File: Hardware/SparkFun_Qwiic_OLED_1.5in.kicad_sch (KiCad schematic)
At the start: 39 parts, among them J1 Qwiic_RA, J2 Qwiic_RA, J3 Conn_01x06, J4 Conn_01x24_FPC, U2 WEO128128ASAP3N00000, U5 AP3012

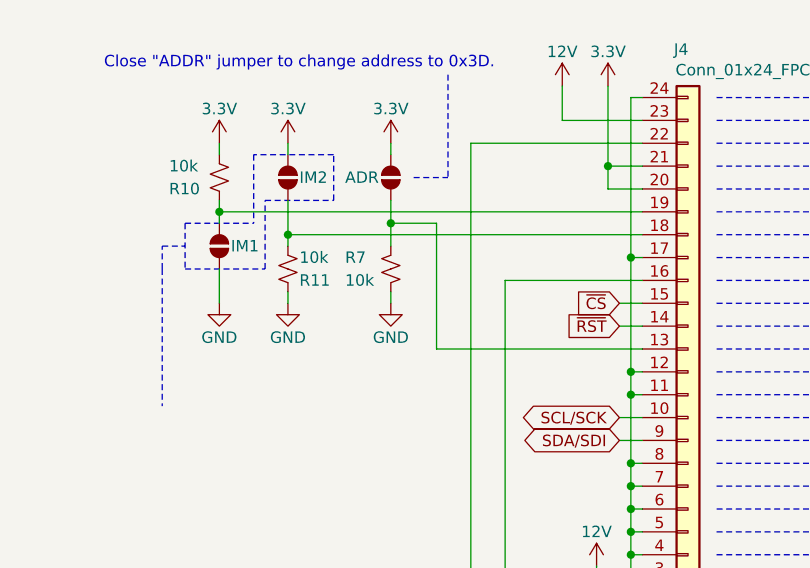
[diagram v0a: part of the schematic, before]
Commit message: Adds no-connect on pin 5, adds prod-id value for 569k resistor
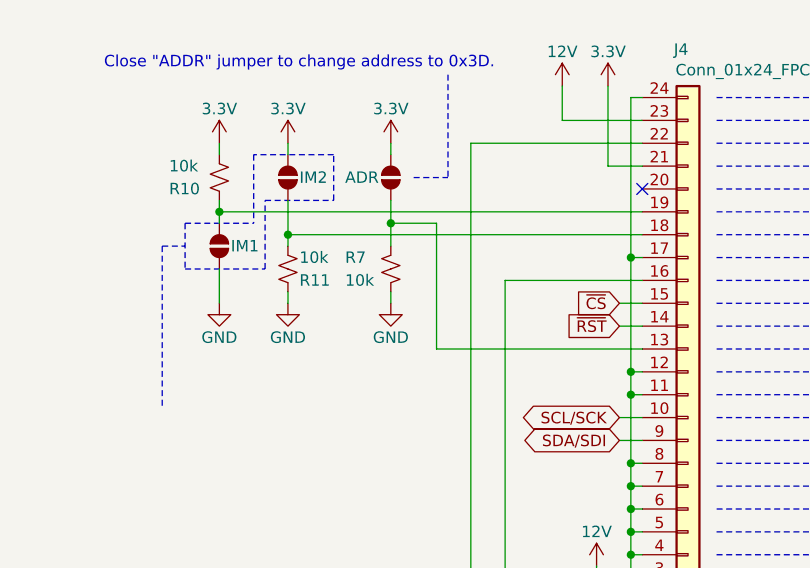
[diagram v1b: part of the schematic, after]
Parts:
- R6: PROD_ID RES-... -> RES-26754
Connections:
- net 3.3V: no longer J4.20 (Pin_20)
- no-connect marks 0 -> 1
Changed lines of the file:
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@@
-	)
-	(junction
-		(at 83.82 44.45)
-		(diameter 0)
-		(color 0 0 0 0)
 	)
 	(junction
@@
 		(color 0 0 0 0)
 	)
+	(no_connect
+		(at 87.63 46.99)
+	)
 	(wire
 		(pts
@@
 	(polyline
 		(pts
-			(xy 34.29 55.88) (xy 34.29 71.12)
+			(xy 34.29 53.34) (xy 34.29 71.12)
 		)
 		(stroke
@@
 	(wire
 		(pts
-			(xy 83.82 46.99) (xy 83.82 44.45)
-		)
-		(stroke
-			(width 0)
-			(type default)
-		)
-	)
-	(wire
-		(pts
 			(xy 83.82 35.56) (xy 83.82 44.45)
 		)
@@
 		)
 	)
-	(polyline
-		(pts
-			(xy 34.29 55.88) (xy 34.29 53.34)
-		)
-		(stroke
-			(width 0)
-			(type dash)
-			(color 132 132 132 1)
-		)
-	)
 	(wire
 		(pts
@@
 			(width 0)
 			(type dash)
-		)
-	)
-	(wire
-		(pts
-			(xy 87.63 46.99) (xy 83.82 46.99)
-		)
-		(stroke
-			(width 0)
-			(type default)
 		)
 	)
@@
 			)
 		)
-		(property "PROD_ID" "RES-..."
+		(property "PROD_ID" "RES-26754"
 			(at 78.74 95.25 0)
 			(effects

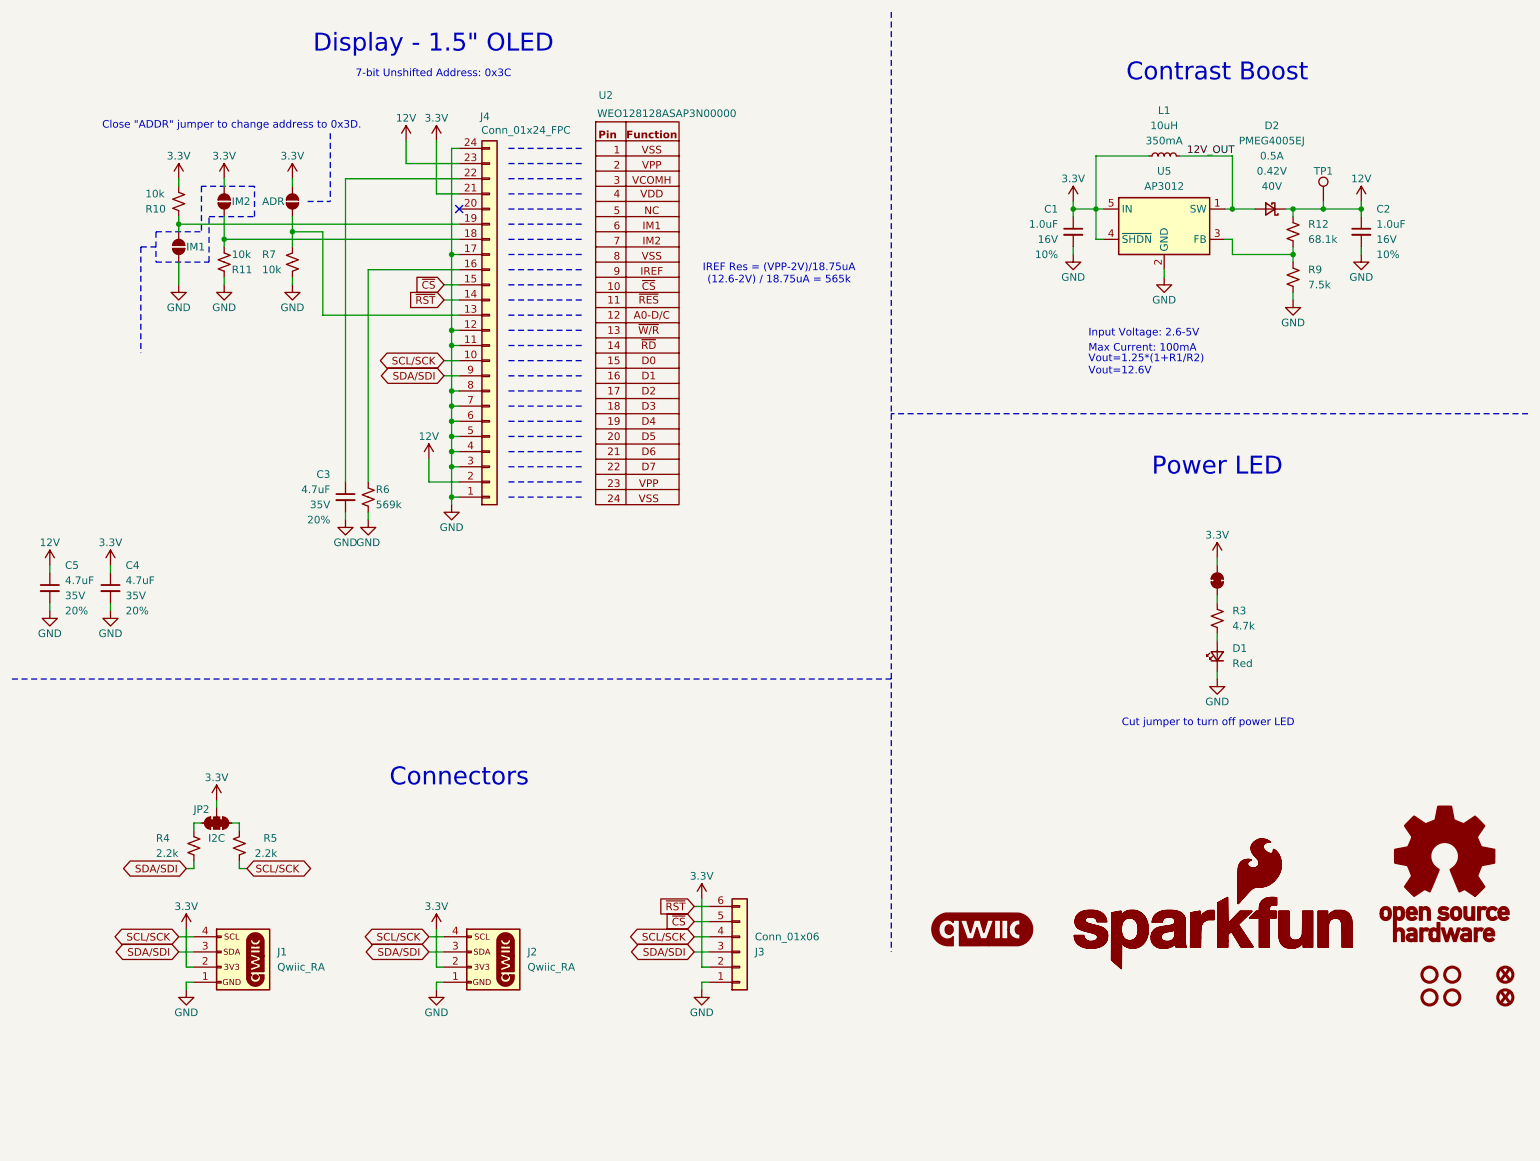
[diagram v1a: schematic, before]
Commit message: Adds D/C to PTH header for SPI funcitonality
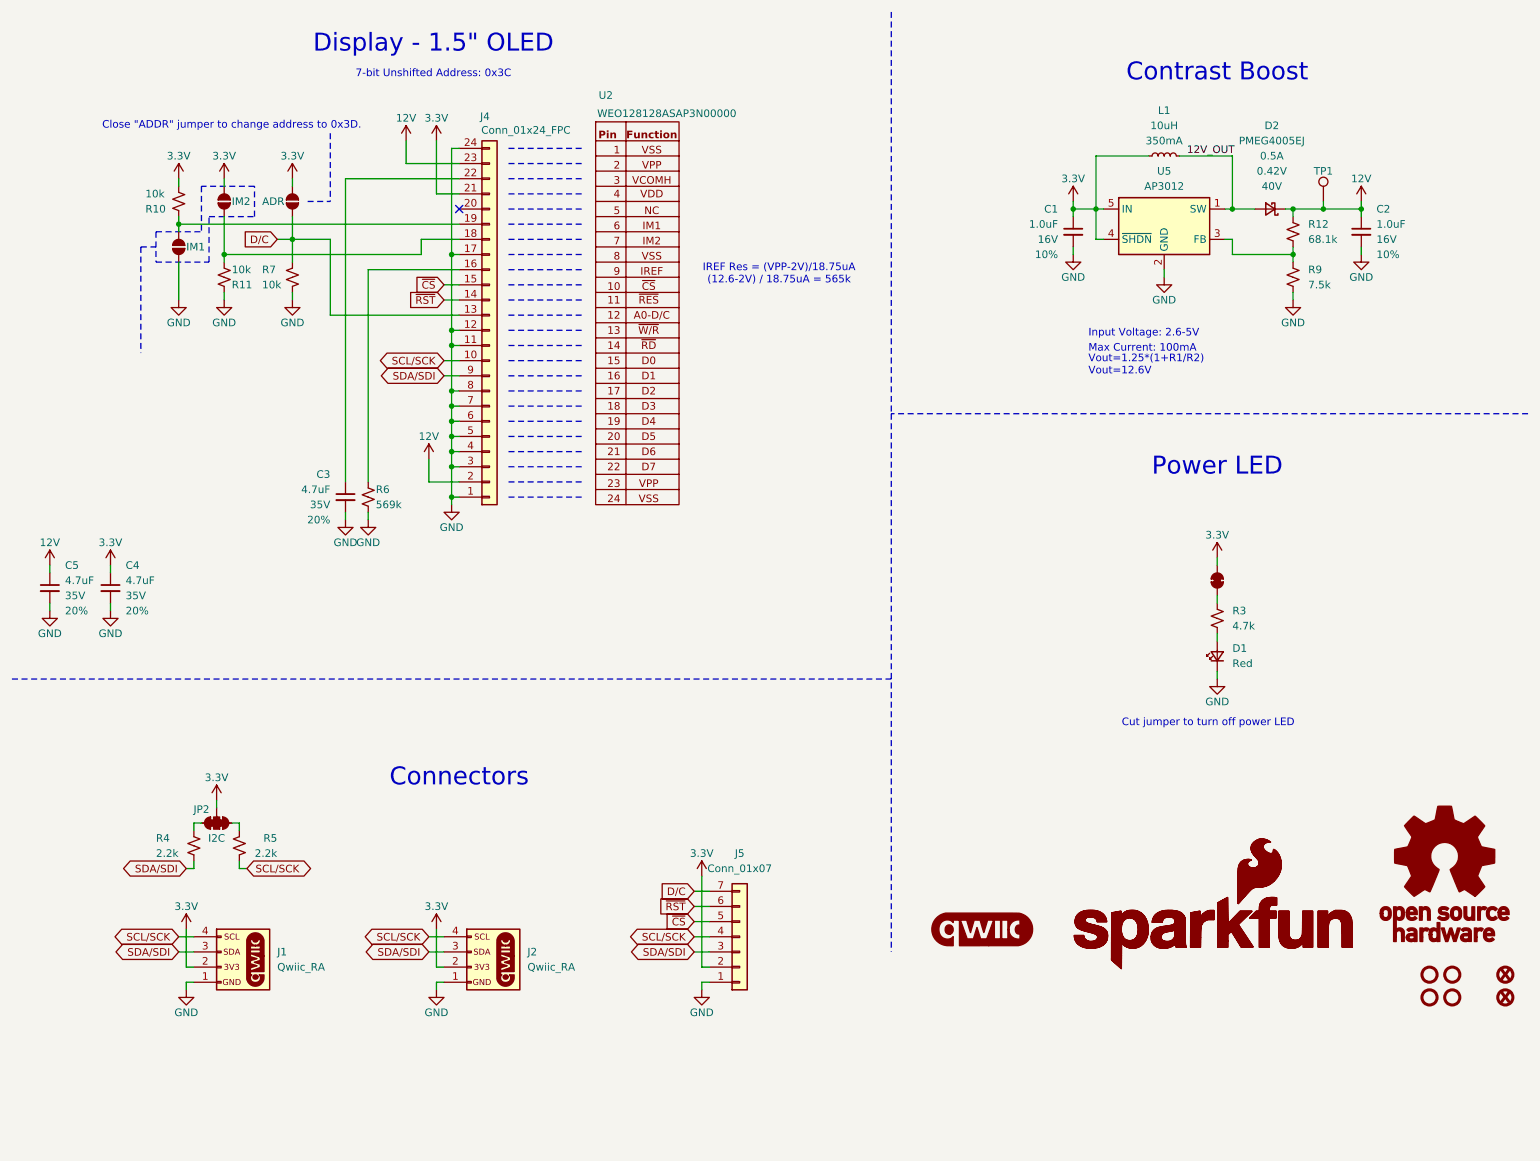
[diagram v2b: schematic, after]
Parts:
- removed J3: Conn_01x06, SparkFun-Connector:1x06, symbol SparkFun-Connector:Conn_01x06
- added J5: Conn_01x07, SparkFun-Connector:1x07, symbol SparkFun-Connector:Conn_01x07
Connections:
- net 3.3V: now also J5.2 (Pin_2)
- net GND: now also J5.1 (Pin_1)
- net SCL/SCK: now also J5.4 (Pin_4)
- net SDA/SDI: now also J5.3 (Pin_3)
- net ~{CS}: now also J5.5 (Pin_5)
- net ~{RST}: now also J5.6 (Pin_6)
- net D/C: now reaches J4.13 (Pin_13), JP3.1 (A), R7.2
- net D/C: now also J5.7 (Pin_7)
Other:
- moved on the sheet: R11, R7

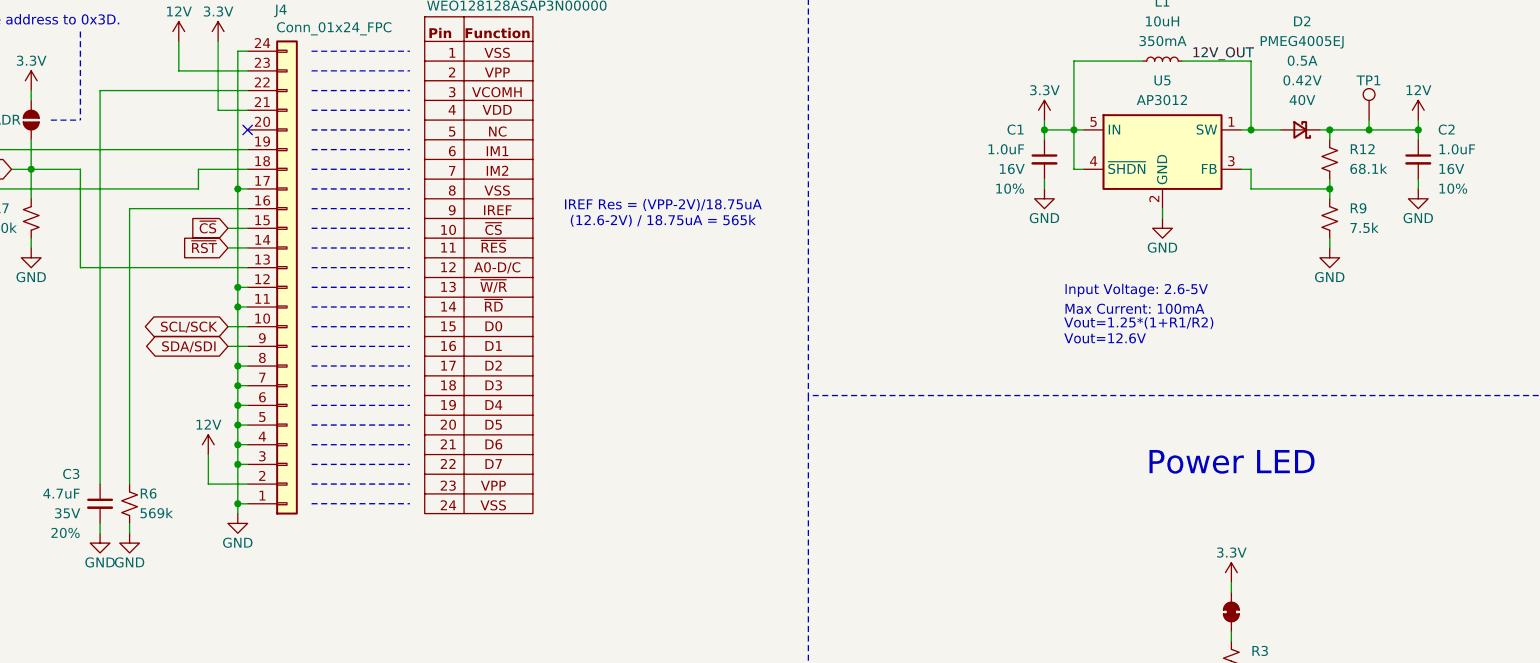
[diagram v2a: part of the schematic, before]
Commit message: Changes certain resistors to use more common values
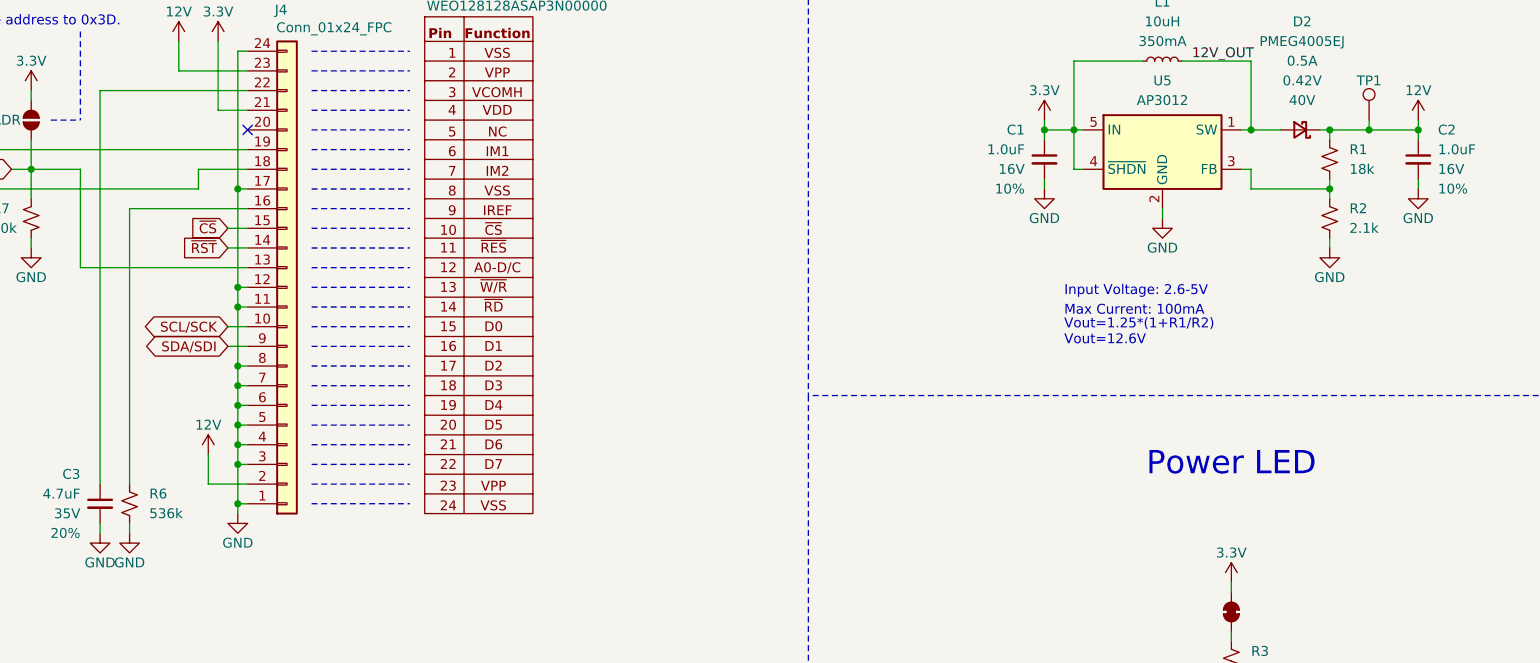
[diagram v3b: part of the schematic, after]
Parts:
- removed R12: 68.1k, SparkFun-Resistor:R_0603_1608Metric, symbol SparkFun-Resistor:68.1k_0603
- removed R6: 569k, SparkFun-Resistor:R_0603_1608Metric, symbol SparkFun-Resistor:634k_0603
- removed R9: 7.5k, SparkFun-Resistor:R_0603_1608Metric, symbol SparkFun-Resistor:7.5k_0603
- added R1: 18k, SparkFun-Resistor:R_0603_1608Metric, symbol SparkFun-Resistor:18k_0603
- added R2: 2.1k, SparkFun-Resistor:R_0603_1608Metric, symbol SparkFun-Resistor:2.1k_0603
- added R6: 536k, SparkFun-Resistor:R_0603_1608Metric, symbol SparkFun-Resistor:536k_0603
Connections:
- net 12V: now also R1.2
- net GND: now also R2.1, R6.1
- net at J4.16 (Pin_16): now also R6.2
- net at U5.3 (FB): now also R1.1, R2.2
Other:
- note removed: "IREF Res = (VPP-2V)/18.75uA (12.6-2V) / 18.75uA = 565k"

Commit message: Updates to v10
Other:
- company: (none) -> SparkFun Electronics
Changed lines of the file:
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@@
 	(title_block
 		(title "SparkFun Qwiic OLED 128x128 1.5in")
-		(date "2025-04-26")
-		(rev "v01")
+		(date "2025-08-06")
+		(rev "v10")
+		(company "SparkFun Electronics")
 		(comment 1 "Designed By: N. Seidle")
 		(comment 2 "Revised By: Elias Santistevan")
@@
 			)
 		)
-		(column_widths 7.62 8.89 13.97)
-		(row_heights 2.54 2.54 2.54)
+		(column_widths 10.16 8.89 13.97)
+		(row_heights 3.81 2.54 2.54 2.54)
 		(cells
 			(table_cell "IM1"
 				(exclude_from_sim no)
 				(at 20.32 71.12 0)
-				(size 7.62 2.54)
+				(size 10.16 3.81)
 				(margins 0.9525 0.9525 0.9525 0.9525)
 				(span 1 1)
@@
 			(table_cell "IM2"
 				(exclude_from_sim no)
-				(at 27.94 71.12 0)
+				(at 30.48 71.12 0)
+				(size 8.89 3.81)
+				(margins 0.9525 0.9525 0.9525 0.9525)
+				(span 1 1)
+				(fill
+					(type none)
+				)
+				(effects
+					(font
+						(size 1.27 1.27)
+					)
+					(justify left top)
+				)
+			)
+			(table_cell "Interface"
+				(exclude_from_sim no)
+				(at 39.37 71.12 0)
+				(size 13.97 3.81)
+				(margins 0.9525 0.9525 0.9525 0.9525)
+				(span 1 1)
+				(fill
+					(type none)
+				)
+				(effects
+					(font
+						(size 1.27 1.27)
+					)
+					(justify left top)
+				)
+			)
+			(table_cell "Open"
+				(exclude_from_sim no)
+				(at 20.32 74.93 0)
+				(size 10.16 2.54)
+				(margins 0.9525 0.9525 0.9525 0.9525)
+				(span 1 1)
+				(fill
+					(type none)
+				)
+				(effects
+					(font
+						(size 1.27 1.27)
+					)
+					(justify left top)
+				)
+			)
+			(table_cell "Open"
+				(exclude_from_sim no)
+				(at 30.48 74.93 0)
 				(size 8.89 2.54)
 				(margins 0.9525 0.9525 0.9525 0.9525)
@@
 				)
 			)
-			(table_cell "Interface"
+			(table_cell "I2C"
 				(exclude_from_sim no)
-				(at 36.83 71.12 0)
+				(at 39.37 74.93 0)
 				(size 13.97 2.54)
 				(margins 0.9525 0.9525 0.9525 0.9525)
@@
 				)
 			)
-			(table_cell "Open"
+			(table_cell "Closed"
 				(exclude_from_sim no)
-				(at 20.32 73.66 0)
-				(size 7.62 2.54)
+				(at 20.32 77.47 0)
+				(size 10.16 2.54)
 				(margins 0.9525 0.9525 0.9525 0.9525)
 				(span 1 1)
@@
 				)
 			)
-			(table_cell "Open"
+			(table_cell "Closed"
 				(exclude_from_sim no)
-				(at 27.94 73.66 0)
+				(at 30.48 77.47 0)
 				(size 8.89 2.54)
 				(margins 0.9525 0.9525 0.9525 0.9525)
@@
 				)
 			)
-			(table_cell "I2C"
+			(table_cell "3-Wire SPI"
 				(exclude_from_sim no)
-				(at 36.83 73.66 0)
+				(at 39.37 77.47 0)
 				(size 13.97 2.54)
 				(margins 0.9525 0.9525 0.9525 0.9525)
@@
 			(table_cell "Closed"
 				(exclude_from_sim no)
-				(at 20.32 76.2 0)
-				(size 7.62 2.54)
+				(at 20.32 80.01 0)
+				(size 10.16 2.54)
 				(margins 0.9525 0.9525 0.9525 0.9525)
 				(span 1 1)
@@
 				)
 			)
-			(table_cell "Closed"
+			(table_cell "Open"
 				(exclude_from_sim no)
-				(at 27.94 76.2 0)
+				(at 30.48 80.01 0)
 				(size 8.89 2.54)
 				(margins 0.9525 0.9525 0.9525 0.9525)
@@
 				)
 			)
-			(table_cell "3-Wire SPI"
+			(table_cell "4-Wire SPI"
 				(exclude_from_sim no)
-				(at 36.83 76.2 0)
+				(at 39.37 80.01 0)
 				(size 13.97 2.54)
 				(margins 0.9525 0.9525 0.9525 0.9525)
